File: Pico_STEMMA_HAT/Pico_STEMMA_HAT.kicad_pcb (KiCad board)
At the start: 2 copper layers, 58 x 67 mm, 66 parts, among them J1 Conn_01x20_Socket, J2 Conn_01x20_Socket, J3 SDCARD_MODULE

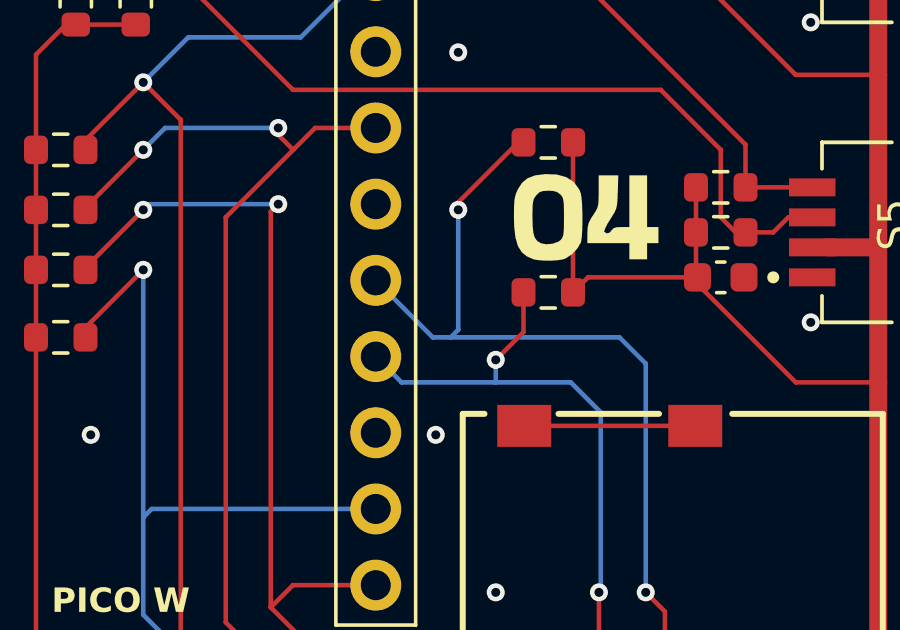
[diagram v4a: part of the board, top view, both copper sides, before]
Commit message: Adjust SD card pin for OCD-reasons
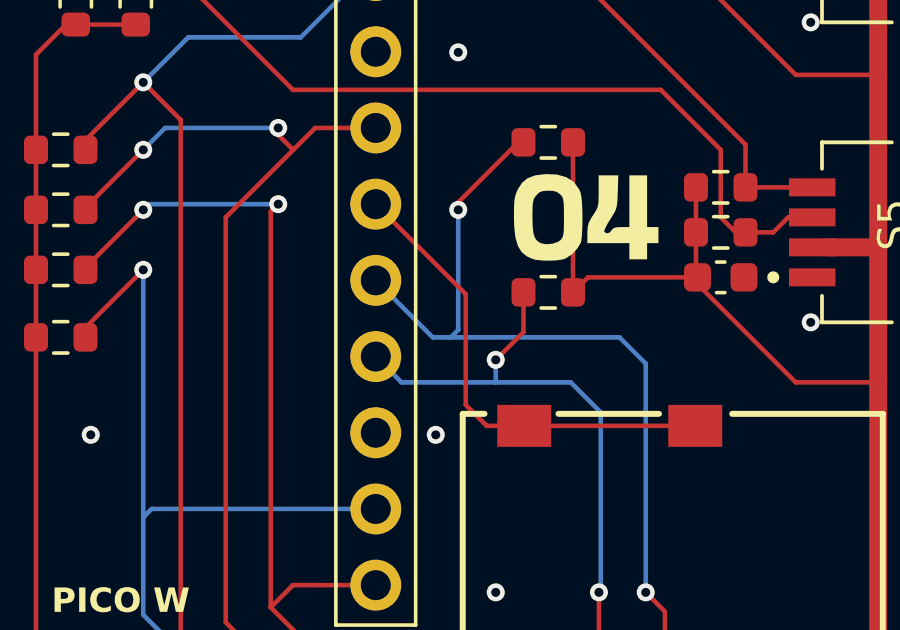
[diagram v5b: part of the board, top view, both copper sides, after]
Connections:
- J1 pad 15: /GPIO20/MISO -> /GPIO20/CD/CARD_DETECT
- J3 pad 10: /GPIO17/CARD_DETECT -> /GPIO20/CD/CARD_DETECT
- J3 pad 9: /GPIO17/CARD_DETECT -> /GPIO20/CD/CARD_DETECT
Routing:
- net /GPIO20/CD/CARD_DETECT: track 0.00 -> 16.1 mm
- net /GPIO17/CARD_DETECT: track 5.90 -> 0.00 mm

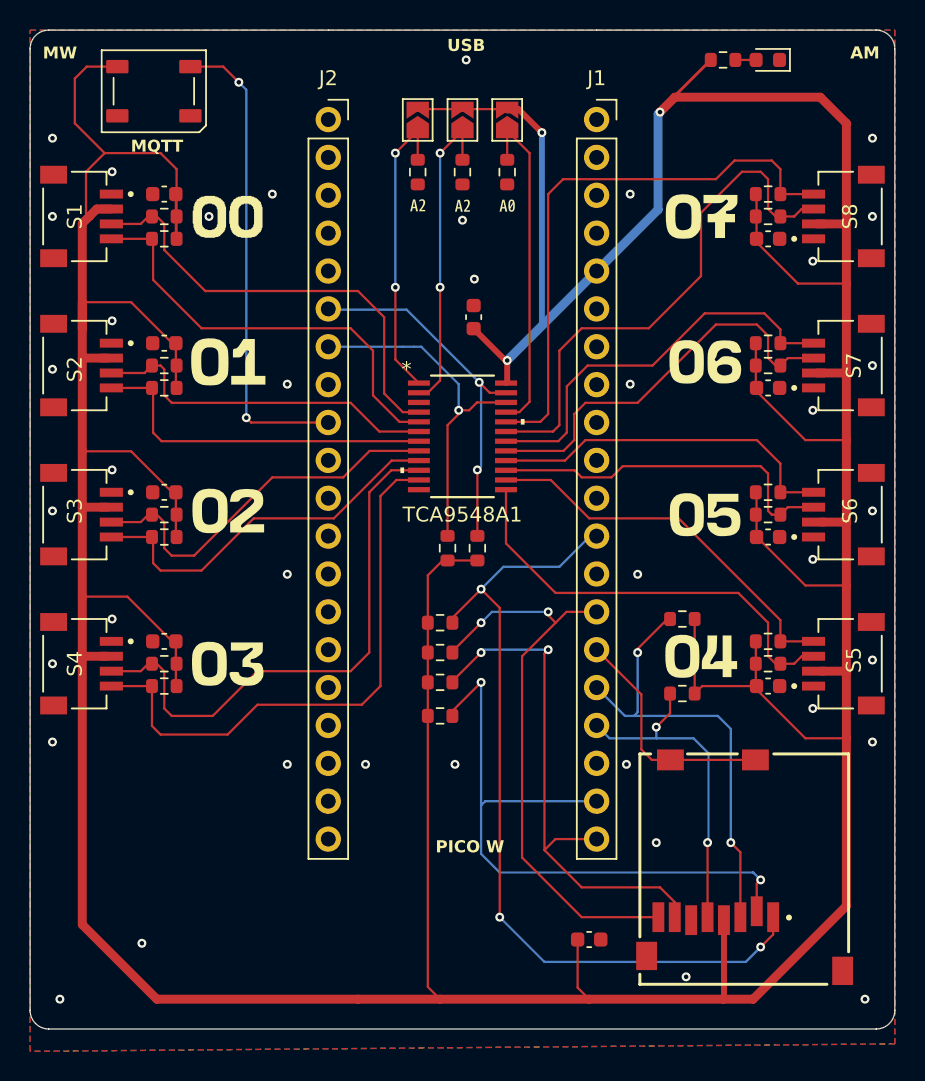
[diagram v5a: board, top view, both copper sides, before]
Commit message: Change reset pin to be out in the open
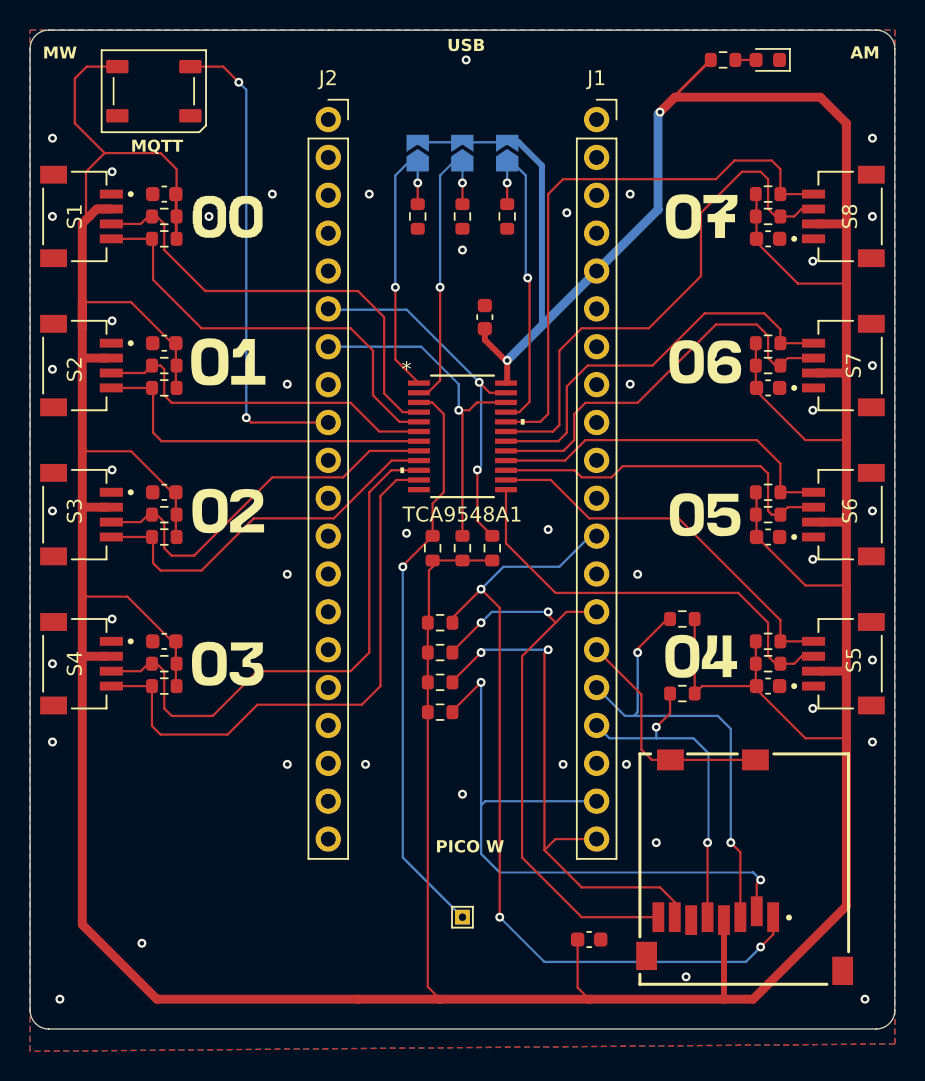
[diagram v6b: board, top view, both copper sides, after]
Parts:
- removed kibuzzard-67A6B8FA: G***, kibuzzard-67A6B8FA
- added R29: 10k, Resistor_SMD:R_0603_1608Metric, F.Cu at (148.0, 107.2)
- added TP1: RESET PIN, TestPoint:TestPoint_THTPad_1.0x1.0mm_Drill0.5mm, F.Cu at (150.0, 132.0)
- added kibuzzard-67A6E024: G***, kibuzzard-67A6E024, B.Cu at (150.0, 83.8)
- JP1, JP2, JP3, kibuzzard-67A6AC81, kibuzzard-67A6B903: moved to B.Cu
- moved R26 2.97 mm to (153.0, 85.0)
- moved R27 2.97 mm to (150.0, 85.0)
- moved R28 2.97 mm to (147.0, 85.0)
- moved JP1 2.22 mm to (153.0, 80.8)
- moved JP2 2.22 mm to (150.0, 80.8)
- moved JP3 2.22 mm to (147.0, 80.8)
- moved R24 1.00 mm to (150.0, 107.2)
- moved R25 1.00 mm to (152.0, 107.2)
- moved C9 0.75 mm to (151.5, 91.8)
- moved kibuzzard-67A6AC81 0.53 mm to (153.0, 83.8), turned to 180 degrees
- moved kibuzzard-67A6B903 0.50 mm to (147.0, 83.8), turned to 180 degrees
- moved R20 0.25 mm to (148.5, 118.2)
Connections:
- TCA9548A1 pad 3: unconnected-(TCA9548A1-#RESET-Pad3) -> /RESET
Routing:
- net /RESET: track 0.00 -> 38.5 mm, vias 0 -> 1
- net +3V3: track 388.6 -> 387.0 mm, vias 3 -> 2
- net /A0: track 22.6 -> 22.1 mm, vias 0 -> 2
- net GND: vias 39 -> 43

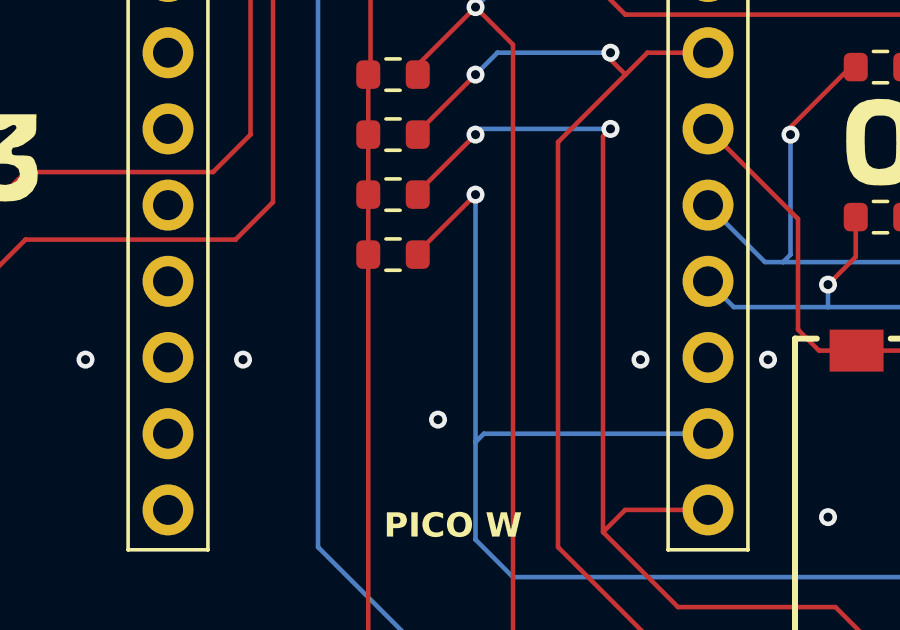
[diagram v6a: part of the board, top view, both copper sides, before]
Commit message: Adjust reset pin trace
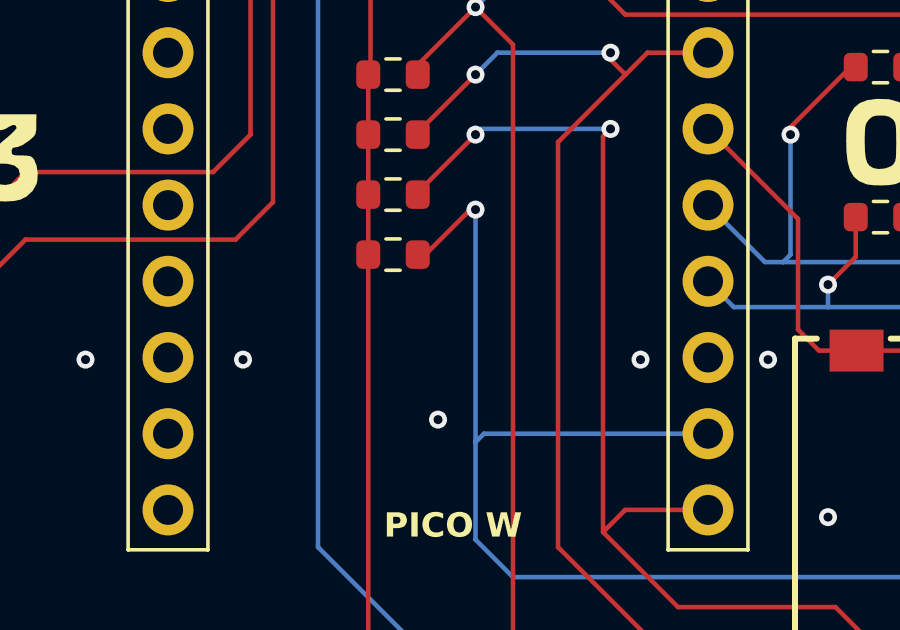
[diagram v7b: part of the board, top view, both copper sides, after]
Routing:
- net /GPIO17/CS: track 44.1 -> 43.2 mm
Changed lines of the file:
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@@
 		)
 		(property "Value" "10k"
-			(at 0 1.43 90)
+			(at 0 0 90)
 			(layer "F.Fab")
 			(effects
@@
 		(tags "resistor")
 		(property "Reference" "R24"
-			(at 0 -1.43 90)
+			(at 0 -1 90)
 			(layer "F.Fab")
 			(effects
@@
 		)
 		(property "Value" "4.7k"
-			(at -3.25 -2.25 90)
+			(at 0 0 90)
 			(layer "F.Fab")
 			(effects
@@
 		(tags "resistor")
 		(property "Reference" "R25"
-			(at 0 -1.43 90)
+			(at 0 1.5 90)
 			(layer "F.Fab")
 			(effects
@@
 		)
 		(property "Value" "4.7k"
-			(at -3.25 -2.25 90)
+			(at 0 0 90)
 			(layer "F.Fab")
 			(effects
@@
 				(font
 					(size 0.001 0.001)
+					(thickness 0.15)
 				)
 				(justify mirror)
@@
 				(font
 					(size 0.001 0.001)
+					(thickness 0.15)
 				)
 				(justify mirror)
@@
 	)
 	(segment
-		(start 148 108.5)
-		(end 147.75 108.75)
-		(width 0.1524)
-		(layer "F.Cu")
-		(net 2)
-	)
-	(segment
 		(start 130.775 113.5)
 		(end 130.775 116.45)
@@
 	)
 	(segment
-		(start 147.75 108.75)
-		(end 147.75 112.175)
-		(width 0.1524)
-		(layer "F.Cu")
-		(net 2)
-	)
-	(segment
 		(start 143 137.5)
 		(end 129.5 137.5)
@@
 	)
 	(segment
-		(start 147.75 112.175)
-		(end 147.675 112.25)
-		(width 0.1524)
-		(layer "F.Cu")
-		(net 2)
-	)
-	(segment
 		(start 166.65625 74.5)
 		(end 164.25 76.90625)
@@
 	)
 	(segment
+		(start 147.75 112.175)
+		(end 147.675 112.25)
+		(width 0.1524)
+		(layer "F.Cu")
+		(net 2)
+	)
+	(segment
 		(start 167.5 137.5)
 		(end 158.5 137.5)
@@
 	)
 	(segment
+		(start 148 108.075)
+		(end 148 108.5)
+		(width 0.1524)
+		(layer "F.Cu")
+		(net 2)
+	)
+	(segment
 		(start 126.2 114.5)
 		(end 124.5 114.5)
@@
 	)
 	(segment
+		(start 148 108.5)
+		(end 147.75 108.75)
+		(width 0.1524)
+		(layer "F.Cu")
+		(net 2)
+	)
+	(segment
 		(start 169.725 96.725)
 		(end 173 100)
@@
 	)
 	(segment
-		(start 148 108.075)
-		(end 148 108.5)
+		(start 147.75 108.75)
+		(end 147.75 112.175)
 		(width 0.1524)
 		(layer "F.Cu")
@@
 	)
 	(segment
-		(start 151.25 116.25)
-		(end 149.325 118.175)
+		(start 151.25 116.75)
+		(end 151.075 116.75)
 		(width 0.1524)
 		(layer "F.Cu")
@@
 	)
 	(segment
-		(start 149.325 118.175)
+		(start 151.075 116.75)
 		(end 149.325 118.5)
 		(width 0.1524)
@@
 	)
 	(via
-		(at 151.25 116.25)
+		(at 151.25 116.75)
 		(size 0.6)
 		(drill 0.3)
@@
 	)
 	(segment
-		(start 151.25 116.25)
+		(start 151.25 116.75)
 		(end 151.25 124.5)
 		(width 0.1524)

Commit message: Add silkscreen appreciation
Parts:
- added G***: LOGO, LOGO, B.Cu at (129.0, 137.8)
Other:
- board text added: "(Future Dr.)!"
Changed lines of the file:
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@@
 		)
 	)
+	(footprint "LOGO"
+		(layer "B.Cu")
+		(at 129 137.75 180)
+		(property "Reference" "G***"
+			(at 0 0 0)
+			(layer "B.SilkS")
+			(hide yes)
+			(effects
+				(font
+					(size 1.5 1.5)
+					(thickness 0.3)
+				)
+				(justify mirror)
+			)
+		)
+		(property "Value" "LOGO"
+			(at 0.75 0 0)
+			(layer "B.SilkS")
+			(hide yes)
+			(effects
+				(font
+					(size 1.5 1.5)
+					(thickness 0.3)
+				)
+				(justify mirror)
+			)
+		)
+		(property "Footprint" ""
+			(at 0 0 0)
+			(layer "B.Fab")
+			(hide yes)
+			(effects
+				(font
+					(size 1.27 1.27)
+					(thickness 0.15)
+				)
+				(justify mirror)
+			)
+		)
+		(property "Datasheet" ""
+			(at 0 0 0)
+			(layer "B.Fab")
+			(hide yes)
+			(effects
+				(font
+					(size 1.27 1.27)
+					(thickness 0.15)
+				)
+				(justify mirror)
+			)
+		)
+		(property "Description" ""
+			(at 0 0 0)
+			(layer "B.Fab")
+			(hide yes)
+			(effects
+				(font
+					(size 1.27 1.27)
+					(thickness 0.15)
+				)
+				(justify mirror)
+			)
+		)
+		(attr board_only exclude_from_pos_files exclude_from_bom)
+		(fp_poly
+			(pts
+				(xy 0.5 -0.15625) (xy 0.5 -0.1875) (xy 0.46875 -0.1875) (xy 0.4375 -0.1875) (xy 0.4375 -0.15625)
+				(xy 0.4375 -0.125) (xy 0.46875 -0.125) (xy 0.5 -0.125)
+			)
+			(stroke
+				(width 0)
+				(type solid)
+			)
+			(fill solid)
+			(layer "B.SilkS")
+		)
+		(fp_poly
+			(pts
+				(xy 0.3125 0.15625) (xy 0.3125 0.125) (xy 0.28125 0.125) (xy 0.25 0.125) (xy 0.25 0.15625) (xy 0.25 0.1875)
+				(xy 0.28125 0.1875) (xy 0.3125 0.1875)
+			)
+			(stroke
+				(width 0)
+				(type solid)
+			)
+			(fill solid)
+			(layer "B.SilkS")
+		)
+		(fp_poly
+			(pts
+				(xy 0.25 0.21875) (xy 0.25 0.1875) (xy 0.21875 0.1875) (xy 0.1875 0.1875) (xy 0.1875 0.21875) (xy 0.1875 0.25)
+				(xy 0.21875 0.25) (xy 0.25 0.25)
+			)
+			(stroke
+				(width 0)
+				(type solid)
+			)
+			(fill solid)
+			(layer "B.SilkS")
+		)
+		(fp_poly
+			(pts
+				(xy 0.1875 -0.21875) (xy 0.1875 -0.25) (xy 0.15625 -0.25) (xy 0.125 -0.25) (xy 0.125 -0.21875) (xy 0.125 -0.1875)
+				(xy 0.15625 -0.1875) (xy 0.1875 -0.1875)
+			)
+			(stroke
+				(width 0)
+				(type solid)
+			)
+			(fill solid)
+			(layer "B.SilkS")
+		)
+		(fp_poly
+			(pts
+				(xy -0.125 -0.21875) (xy -0.125 -0.25) (xy -0.15625 -0.25) (xy -0.1875 -0.25) (xy -0.1875 -0.21875)
+				(xy -0.1875 -0.1875) (xy -0.15625 -0.1875) (xy -0.125 -0.1875)
+			)
+			(stroke
+				(width 0)
+				(type solid)
+			)
+			(fill solid)
+			(layer "B.SilkS")
+		)
+		(fp_poly
+			(pts
+				(xy 0.375 0.03125) (xy 0.375 -0.0625) (xy 0.40625 -0.0625) (xy 0.4375 -0.0625) (xy 0.4375 -0.09375)
+				(xy 0.4375 -0.125) (xy 0.40625 -0.125) (xy 0.375 -0.125) (xy 0.375 -0.21875) (xy 0.375 -0.3125)
+				(xy 0.34375 -0.3125) (xy 0.3125 -0.3125) (xy 0.3125 -0.34375) (xy 0.3125 -0.375) (xy 0.28125 -0.375)
+				(xy 0.25 -0.375) (xy 0.25 -0.40625) (xy 0.25 -0.4375) (xy 0.28125 -0.4375) (xy 0.3125 -0.4375) (xy 0.3125 -0.46875)
+				(xy 0.3125 -0.5) (xy 0.25 -0.5) (xy 0.1875 -0.5) (xy 0.1875 -0.46875) (xy 0.1875 -0.4375) (xy 0 -0.4375)
+				(xy -0.1875 -0.4375) (xy -0.1875 -0.46875) (xy -0.1875 -0.5) (xy -0.25 -0.5) (xy -0.3125 -0.5) (xy -0.3125 -0.46875)
+				(xy -0.3125 -0.4375) (xy -0.28125 -0.4375) (xy -0.25 -0.4375) (xy -0.25 -0.40625) (xy -0.25 -0.375)
+				(xy -0.28125 -0.375) (xy -0.3125 -0.375) (xy -0.3125 -0.34375) (xy -0.3125 -0.3125) (xy -0.28125 -0.3125)
+				(xy -0.25 -0.3125) (xy -0.25 -0.34375) (xy -0.25 -0.375) (xy 0 -0.375) (xy 0.25 -0.375) (xy 0.25 -0.34375)
+				(xy 0.25 -0.3125) (xy 0.28125 -0.3125) (xy 0.3125 -0.3125) (xy 0.3125 -0.09375) (xy 0.3125 0.125)
+				(xy 0.34375 0.125) (xy 0.375 0.125)
+			)
+			(stroke
+				(width 0)
+				(type solid)
+			)
+			(fill solid)
+			(layer "B.SilkS")
+		)
+		(fp_poly
+			(pts
+				(xy 0.0625 0.46875) (xy 0.0625 0.4375) (xy 0.03125 0.4375) (xy 0 0.4375) (xy 0 0.40625) (xy 0 0.375)
+				(xy 0.03125 0.375) (xy 0.0625 0.375) (xy 0.0625 0.40625) (xy 0.0625 0.4375) (xy 0.09375 0.4375)
+				(xy 0.125 0.4375) (xy 0.125 0.40625) (xy 0.125 0.375) (xy 0.09375 0.375) (xy 0.0625 0.375) (xy 0.0625 0.34375)
+				(xy 0.0625 0.3125) (xy 0.125 0.3125) (xy 0.1875 0.3125) (xy 0.1875 0.28125) (xy 0.1875 0.25) (xy 0.125 0.25)
+				(xy 0.0625 0.25) (xy 0.0625 0.1875) (xy 0.0625 0.125) (xy 0 0.125) (xy -0.0625 0.125) (xy -0.0625 0.15625)
+				(xy -0.0625 0.1875) (xy -0.03125 0.1875) (xy 0 0.1875) (xy 0 0.21875) (xy 0 0.25) (xy -0.09375 0.25)
+				(xy -0.1875 0.25) (xy -0.1875 0.21875) (xy -0.1875 0.1875) (xy -0.21875 0.1875) (xy -0.25 0.1875)
+				(xy -0.25 0.15625) (xy -0.25 0.125) (xy -0.28125 0.125) (xy -0.3125 0.125) (xy -0.3125 -0.09375)
+				(xy -0.3125 -0.3125) (xy -0.34375 -0.3125) (xy -0.375 -0.3125) (xy -0.375 -0.21875) (xy -0.375 -0.125)
+				(xy -0.40625 -0.125) (xy -0.4375 -0.125) (xy -0.4375 -0.15625) (xy -0.4375 -0.1875) (xy -0.46875 -0.1875)
+				(xy -0.5 -0.1875) (xy -0.5 -0.15625) (xy -0.5 -0.125) (xy -0.46875 -0.125) (xy -0.4375 -0.125) (xy -0.4375 -0.09375)
+				(xy -0.4375 -0.0625) (xy -0.40625 -0.0625) (xy -0.375 -0.0625) (xy -0.375 0.03125) (xy -0.375 0.125)
+				(xy -0.34375 0.125) (xy -0.3125 0.125) (xy -0.3125 0.15625) (xy -0.3125 0.1875) (xy -0.28125 0.1875)
+				(xy -0.25 0.1875) (xy -0.25 0.21875) (xy -0.25 0.25) (xy -0.21875 0.25) (xy -0.1875 0.25) (xy -0.1875 0.28125)
+				(xy -0.1875 0.3125) (xy -0.09375 0.3125) (xy 0 0.3125) (xy 0 0.34375) (xy 0 0.375) (xy -0.03125 0.375)
+				(xy -0.0625 0.375) (xy -0.0625 0.40625) (xy -0.0625 0.4375) (xy -0.03125 0.4375) (xy 0 0.4375) (xy 0 0.46875)
+				(xy 0 0.5) (xy 0.03125 0.5) (xy 0.0625 0.5)
+			)
+			(stroke
+				(width 0)
+				(type solid)
+			)
+			(fill solid)
+			(layer "B.SilkS")
+		)
+	)
 	(footprint "Jumper:SolderJumper-2_P1.3mm_Open_TrianglePad1.0x1.5mm"
 		(layer "B.Cu")
@@
 	)
 	(gr_text "Desgined by\nArmando Martinez\n\nCapstone Project for \nMary Etta West"
+		(locked yes)
 		(at 150 137.75 0)
 		(layer "B.SilkS")
@@
 		)
 	)
+	(gr_text "(Future Dr.)!"
+		(at 144.75 138.5 0)
+		(layer "B.SilkS")
+		(effects
+			(font
+				(size 0.52 0.52)
+				(thickness 0.127)
+				(bold yes)
+			)
+			(justify left bottom mirror)
+		)
+	)
 	(gr_text "USB"
 		(at 150.25 74 0)
@@
 		(net 1)
 		(net_name "GND")
+		(locked yes)
 		(layers "F&B.Cu")
 		(hatch edge 0.5)
